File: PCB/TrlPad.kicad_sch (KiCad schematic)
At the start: 26 parts, among them SW1 SW_Push, SW2 SW_Push, SW3 SW_Push, SW4 SW_Push, SW5 RotaryEncoder_Switch, U1 XIAO-nRF52840-SMD, U2 128x32_OLED_S

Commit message: v0.1
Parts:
- removed H1, H2, H3, H4: break off, MountingHole:MountingHole_3.2mm_M3, symbol Mechanical:MountingHole
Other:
- note removed: "Mounting Holes"

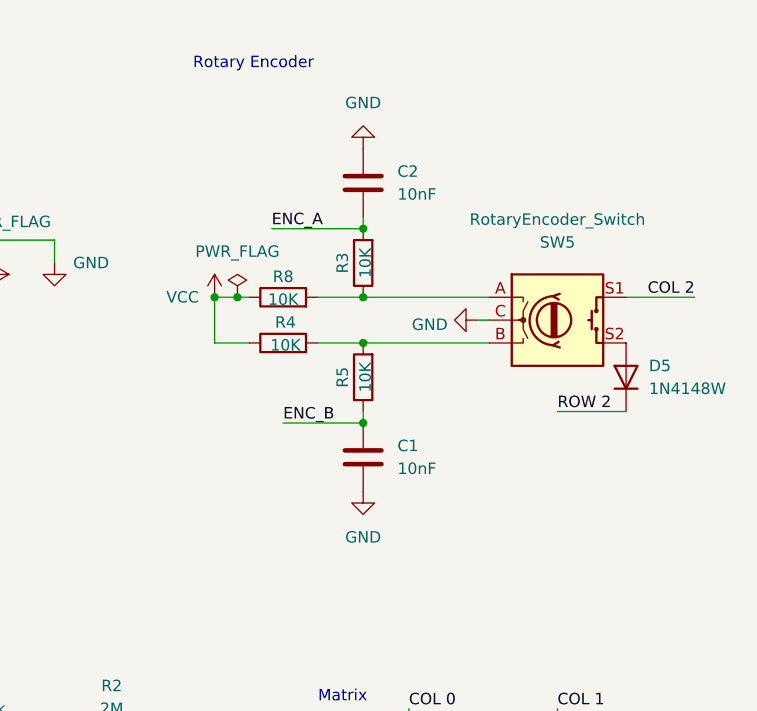
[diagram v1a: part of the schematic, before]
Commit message: Updated BOM + fixed PCB
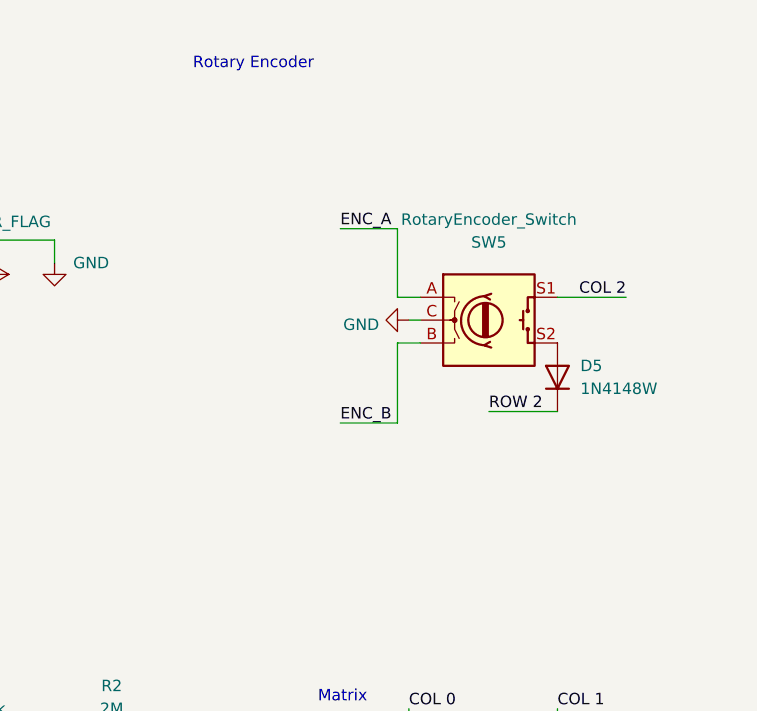
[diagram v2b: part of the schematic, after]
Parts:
- removed C1, C2: 10nF, Capacitor_SMD:C_0603_1608Metric_Pad1.08x0.95mm_HandSolder, symbol Device:C
- removed R3, R4, R5, R8: 10K, Resistor_SMD:R_0603_1608Metric_Pad0.98x0.95mm_HandSolder, symbol Device:R
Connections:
- net ENC_A: now also SW5.A
- net ENC_B: now also SW5.B
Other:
- moved on the sheet: D5, SW5
